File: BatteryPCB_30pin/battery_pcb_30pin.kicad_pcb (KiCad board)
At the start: 2 copper layers, 145.3 x 142.5 mm, 53 parts, among them J1 ESP32 left, J2 ESP32 right, J3 RunCam Split 4, J5 to COTS altimeter, J6 to SRAD flight computer, Q1 AO3407A, SW1 CAM POWER, SW2 COTS ARM, SW3 SRAD ARM, U1 LMR51430XFDDCR

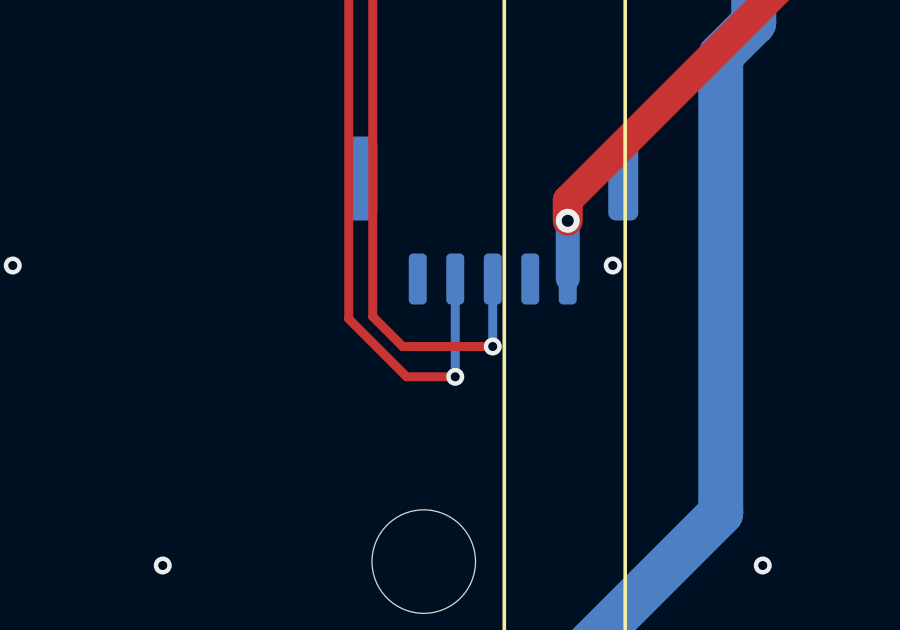
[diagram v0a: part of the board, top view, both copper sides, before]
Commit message: Battery PCB 30-pin: J3 pin order matches the RunCam Split 4 pads
J3 pins 3 and 5 swapped (3 = CAM_VIDEO, 5 = CAM_RX), so J3 pin 1..5 =
VCC, GND, Video, TX, RX, the camera's own pad order: the camera harness
is now a straight cable with no crossed wires.

- Schematic sheet 3 and the board pad nets updated; CAM_RX now drops to
  the back right beside pin 5 (route 2.5 mm shorter, old via removed).
- Back-silk legend reads 3 VID / 4 TX / 5 RX; README harness table, BOM
  camera note and hand-fit list updated; Gerbers, order-package zip,
  schematic PDF, project zip and STEP regenerated.
- ERC 0 errors, DRC 0 (schematic parity, zones refilled, same 3
  exclusions), verify_A unchanged, all 27 CPL placements re-checked.

BatteryPCB (the 38-pin board) keeps its old J3 order.

Co-Authored-By: Claude Opus 5.5 <noreply@anthropic.com>
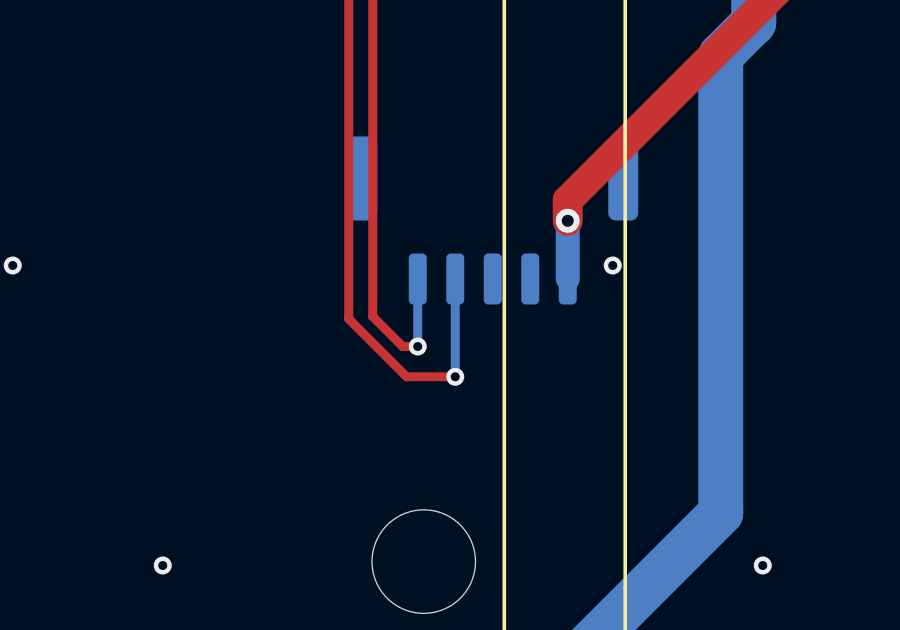
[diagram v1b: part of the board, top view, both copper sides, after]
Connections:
- J3 pad 3: /3. ESP32 + camera/CAM_RX -> /3. ESP32 + camera/CAM_VIDEO
- J3 pad 5: /3. ESP32 + camera/CAM_VIDEO -> /3. ESP32 + camera/CAM_RX
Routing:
- net /3. ESP32 + camera/CAM_RX: track 43.8 -> 41.3 mm
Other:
- board text added: "1 +5V 2 GND 3 VID 4 TX 5 RX"
- board text removed: "1 +5V 2 GND 3 RX 4 TX 5 VID"
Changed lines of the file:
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@@
 			(layers "B.Cu" "B.Mask" "B.Paste")
 			(roundrect_rratio 0.25)
-			(net "/3. ESP32 + camera/CAM_RX")
+			(net "/3. ESP32 + camera/CAM_VIDEO")
 			(pinfunction "Pin_3_3")
 			(pintype "passive")
@@
 			(layers "B.Cu" "B.Mask" "B.Paste")
 			(roundrect_rratio 0.25)
-			(net "/3. ESP32 + camera/CAM_VIDEO")
+			(net "/3. ESP32 + camera/CAM_RX")
 			(pinfunction "Pin_5_5")
 			(pintype "passive")
@@
 		)
 	)
-	(gr_text "1 +5V  2 GND\n3 RX  4 TX  5 VID"
+	(gr_text "1 +5V  2 GND\n3 VID  4 TX  5 RX"
 		(at 151.5 177.7 0)
 		(layer "B.SilkS")
@@
 	)
 	(segment
-		(start 142 135.845)
-		(end 142 171.7)
+		(start 141.2 138.395)
+		(end 141.2 171.78)
 		(width 0.3)
 		(layer "F.Cu")
-		(net "/3. ESP32 + camera/CAM_RX")
+		(net "/3. ESP32 + camera/CAM_TX")
 	)
 	(segment
-		(start 142 171.7)
-		(end 143 172.7)
+		(start 141.2 171.78)
+		(end 143.13 173.71)
 		(width 0.3)
 		(layer "F.Cu")
-		(net "/3. ESP32 + camera/CAM_RX")
+		(net "/3. ESP32 + camera/CAM_TX")
 	)
 	(segment
-		(start 143 172.7)
-		(end 146 172.7)
+		(start 143.13 173.71)
+		(end 144.75 173.71)
 		(width 0.3)
 		(layer "F.Cu")
-		(net "/3. ESP32 + camera/CAM_RX")
+		(net "/3. ESP32 + camera/CAM_TX")
 	)
 	(via
-		(at 142 135.845)
+		(at 144.75 173.71)
 		(size 0.6)
 		(drill 0.3)
 		(layers "F.Cu" "B.Cu")
-		(net "/3. ESP32 + camera/CAM_RX")
+		(net "/3. ESP32 + camera/CAM_TX")
 	)
 	(via
-		(at 146 172.7)
+		(at 141.2 138.395)
 		(size 0.6)
 		(drill 0.3)
 		(layers "F.Cu" "B.Cu")
-		(net "/3. ESP32 + camera/CAM_RX")
+		(net "/3. ESP32 + camera/CAM_TX")
 	)
 	(segment
-		(start 146 172.7)
-		(end 146 170.45)
+		(start 142.975 137.74)
+		(end 141.855 137.74)
 		(width 0.3)
 		(layer "B.Cu")
-		(net "/3. ESP32 + camera/CAM_RX")
+		(net "/3. ESP32 + camera/CAM_TX")
 	)
 	(segment
-		(start 142.975 135.2)
-		(end 142.645 135.2)
+		(start 141.855 137.74)
+		(end 141.2 138.395)
 		(width 0.3)
 		(layer "B.Cu")
-		(net "/3. ESP32 + camera/CAM_RX")
+		(net "/3. ESP32 + camera/CAM_TX")
 	)
 	(segment
-		(start 142.645 135.2)
-		(end 142 135.845)
+		(start 144.75 173.71)
+		(end 144.75 170.45)
 		(width 0.3)
 		(layer "B.Cu")
-		(net "/3. ESP32 + camera/CAM_RX")
+		(net "/3. ESP32 + camera/CAM_TX")
 	)
 	(segment
-		(start 141.2 138.395)
-		(end 141.2 171.78)
+		(start 142 135.845)
+		(end 142 171.7)
 		(width 0.3)
 		(layer "F.Cu")
-		(net "/3. ESP32 + camera/CAM_TX")
+		(net "/3. ESP32 + camera/CAM_RX")
 	)
 	(segment
-		(start 141.2 171.78)
-		(end 143.13 173.71)
+		(start 142 171.7)
+		(end 143 172.7)
 		(width 0.3)
 		(layer "F.Cu")
-		(net "/3. ESP32 + camera/CAM_TX")
+		(net "/3. ESP32 + camera/CAM_RX")
 	)
 	(segment
-		(start 143.13 173.71)
-		(end 144.75 173.71)
+		(start 143 172.7)
+		(end 143.5 172.7)
 		(width 0.3)
 		(layer "F.Cu")
-		(net "/3. ESP32 + camera/CAM_TX")
+		(net "/3. ESP32 + camera/CAM_RX")
 	)
 	(via
-		(at 144.75 173.71)
+		(at 142 135.845)
 		(size 0.6)
 		(drill 0.3)
 		(layers "F.Cu" "B.Cu")
-		(net "/3. ESP32 + camera/CAM_TX")
+		(net "/3. ESP32 + camera/CAM_RX")
 	)
 	(via
-		(at 141.2 138.395)
+		(at 143.5 172.7)
 		(size 0.6)
 		(drill 0.3)
 		(layers "F.Cu" "B.Cu")
-		(net "/3. ESP32 + camera/CAM_TX")
+		(net "/3. ESP32 + camera/CAM_RX")
 	)
 	(segment
-		(start 142.975 137.74)
-		(end 141.855 137.74)
+		(start 143.5 172.7)
+		(end 143.5 170.45)
 		(width 0.3)
 		(layer "B.Cu")
-		(net "/3. ESP32 + camera/CAM_TX")
+		(net "/3. ESP32 + camera/CAM_RX")
 	)
 	(segment
-		(start 141.855 137.74)
-		(end 141.2 138.395)
+		(start 142.975 135.2)
+		(end 142.645 135.2)
 		(width 0.3)
 		(layer "B.Cu")
-		(net "/3. ESP32 + camera/CAM_TX")
+		(net "/3. ESP32 + camera/CAM_RX")
 	)
 	(segment
-		(start 144.75 173.71)
-		(end 144.75 170.45)
+		(start 142.645 135.2)
+		(end 142 135.845)
 		(width 0.3)
 		(layer "B.Cu")
-		(net "/3. ESP32 + camera/CAM_TX")
+		(net "/3. ESP32 + camera/CAM_RX")
 	)
 	(segment

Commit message: Battery PCB 30-pin: test-point block on the right edge (5V, GND, COTS +/-, SRAD +/-)
Six through-hole test points together on the front right edge, between
the right rod's washer keep-out and the lower zip-tie cut-out, labelled
on the silk: top row TP1 +5V, TP5 COTS +, TP7 SRAD +; bottom row TP3 GND,
TP6 COTS -, TP8 SRAD -.

- TP1/TP3 moved out of the BT3/BT4 gap (hard to reach with cells in).
- TP5-TP8 are new (schematic sheet 4): the COTS and SRAD cells are
  isolated from GND, so each gets its own + / - pair, before the pin
  switch, so they read the cell whether armed or not.
- Routing: +5V from J1-15 (front, via at (44, 2), back); COTS/SRAD +
  from the top tabs down a channel beside BT4; COTS - (front) and
  SRAD - (back) from the bottom tabs under the zip-tie cut-out. Battery
  traces 1.0 mm (Pyro rules), +5V 0.8 mm.
- GND stitching: 3 vias removed where the block sits, 4 nudged <= 0.7 mm
  for clearance. Old TP1 feed removed; 'for zipties' label moved.
- verify_A checks all eight test points; README, layout notes and the
  order package's assembly scope updated; Gerbers, PDF, project zip and
  STEP regenerated. BOM and JLC files unchanged (test points are pads).

ERC 0 errors, DRC 0 (schematic parity, zones refilled, same 3
documented exclusions). No other part, trace or dimension changed.

Co-Authored-By: Claude Opus 5.5 <noreply@anthropic.com>
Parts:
- added TP5: TP_COTS+, TestPoint:TestPoint_THTPad_D2.0mm_Drill1.0mm, F.Cu at (206.5, 165.5)
- added TP6: TP_COTS-, TestPoint:TestPoint_THTPad_D2.0mm_Drill1.0mm, F.Cu at (206.5, 170.5)
- added TP7: TP_SRAD+, TestPoint:TestPoint_THTPad_D2.0mm_Drill1.0mm, F.Cu at (211.5, 165.5)
- added TP8: TP_SRAD-, TestPoint:TestPoint_THTPad_D2.0mm_Drill1.0mm, F.Cu at (211.5, 170.5)
- moved TP1 29.3 mm to (201.5, 165.5)
- moved TP3 27.7 mm to (201.5, 170.5)
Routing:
- net /4. COTS / SRAD supplies/COTS_BAT+: track 25.3 -> 118.7 mm
- net /4. COTS / SRAD supplies/SRAD_BAT+: track 14.3 -> 87.2 mm
- net /4. COTS / SRAD supplies/COTS_BAT-: track 17.7 -> 73.7 mm
- net /4. COTS / SRAD supplies/SRAD_BAT-: track 9.97 -> 45.9 mm, vias 0 -> 1
- net /2. Buck to 5 V/+5V: track 70.5 -> 102.5 mm, vias 3 -> 4
- net GND: vias 108 -> 105
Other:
- board text added: "COTS+"
- board text added: "COTS-"
- board text added: "SRAD+"
- board text added: "SRAD-"

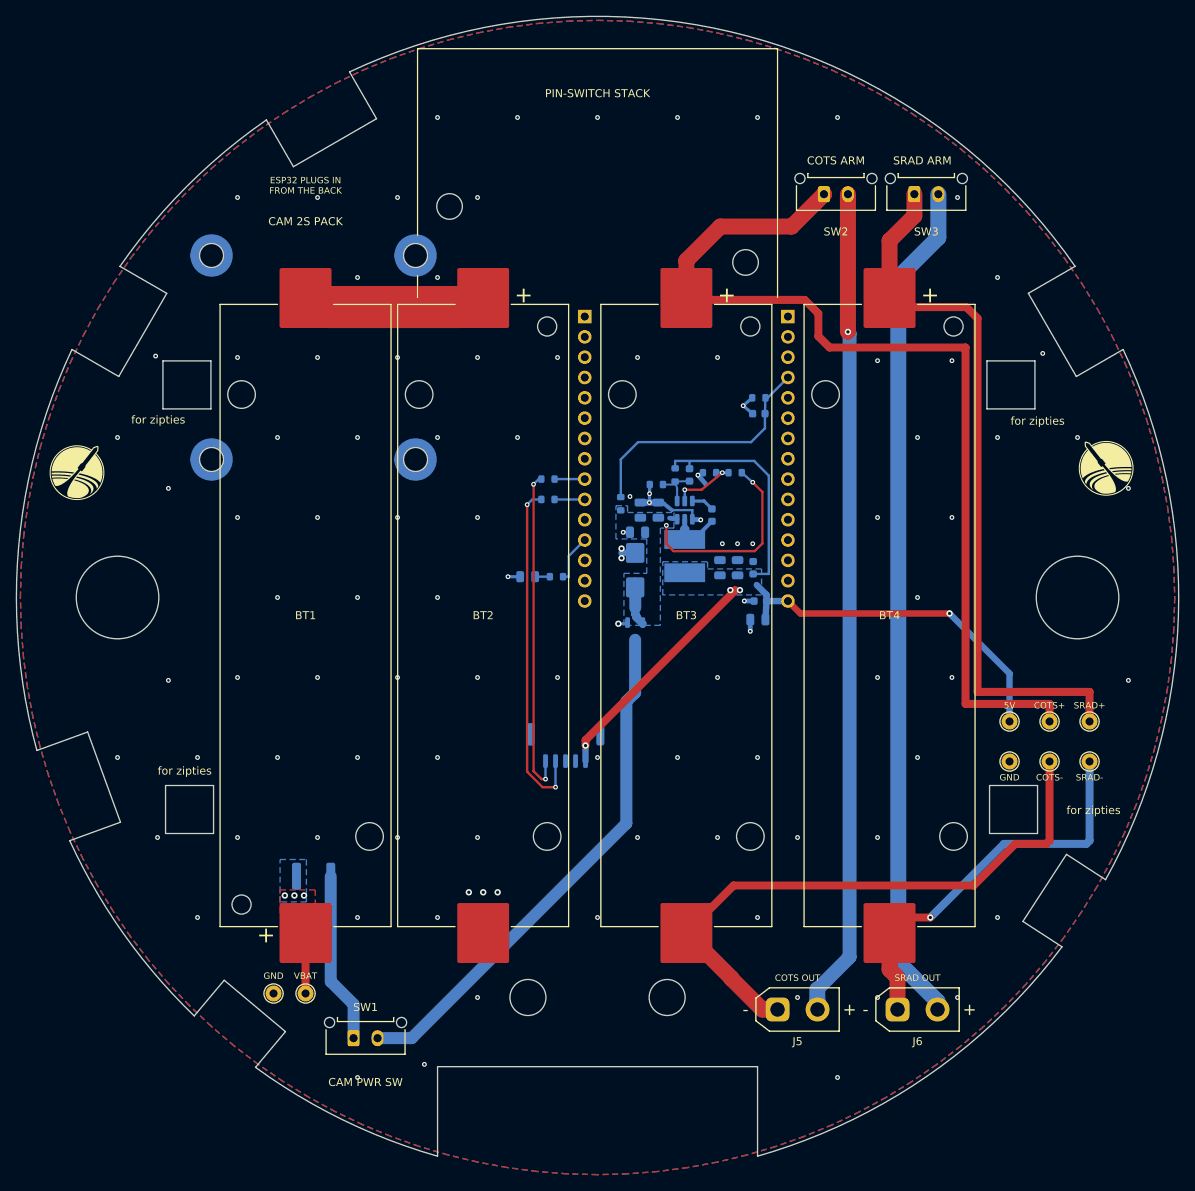
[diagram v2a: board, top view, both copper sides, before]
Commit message: Battery PCB 30-pin: XT30 and battery-holder holes to the datasheets; notes, check script
- XT30 J5/J6 pin holes 1.8 -> 1.9 mm (Amass drawing: 1.9 mm for the
  1.6 mm pins); 0.55 mm copper ring left on the 3.0 mm pads.
- Keystone 1042 holder peg holes 3.45 -> 3.5 mm and locator hole
  2.39 -> 2.4 mm on BT1-BT4 (Keystone M65p27; positions unchanged).
  Footprints updated in battery_pcb.pretty and on the board.
- Only those 16 hole sizes changed on the board: no part, trace, via,
  outline or silk moved. Tightest new gap: COTS_SW to a BT4 peg hole
  0.375 mm (rule 0.3).
- Schematic notes brought up to date: Q1 drop ~0.05 V (was 0.35 V from
  the old diode), J5/J6 are XT30 not Micro-Fit, C9/C10 sit at the
  ESP32's VIN (J1-15).
- verify_A: the old "seven edge cut-outs" count is replaced by a real
  check (7 rim notches + 4 square zip-tie cut-outs); ALL PASS, 36 checks.
- Gerbers, order-package zip, schematic PDF, project zip and STEP
  regenerated; BOM and CPL unchanged.

ERC 0 errors, DRC 0 (schematic parity, zones refilled, same 3
documented exclusions).

Co-Authored-By: Claude Opus 5.5 <noreply@anthropic.com>
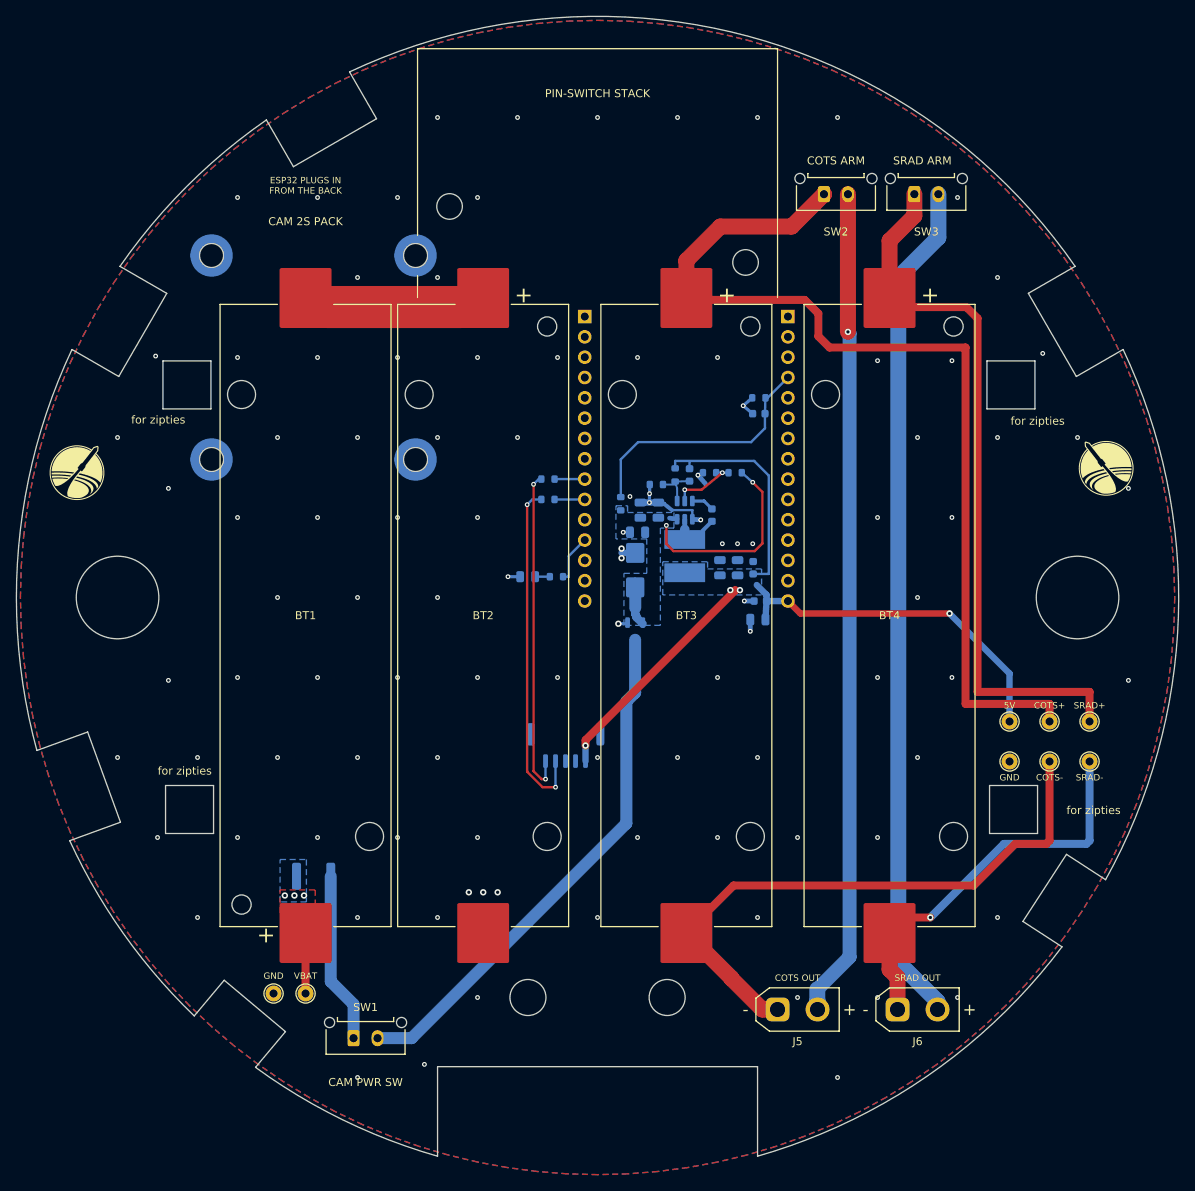
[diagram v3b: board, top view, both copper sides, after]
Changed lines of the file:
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@@
 		(pad "" np_thru_hole circle
 			(at -36.13 -8 90)
-			(size 2.39 2.39)
-			(drill 2.39)
+			(size 2.4 2.4)
+			(drill 2.4)
 			(layers "*.Cu" "*.Mask")
 		)
 		(pad "" np_thru_hole circle
 			(at -27.62 8 90)
-			(size 3.45 3.45)
-			(drill 3.45)
+			(size 3.5 3.5)
+			(drill 3.5)
 			(layers "*.Cu" "*.Mask")
 		)
 		(pad "" np_thru_hole circle
 			(at 27.62 -8 90)
-			(size 3.45 3.45)
-			(drill 3.45)
+			(size 3.5 3.5)
+			(drill 3.5)
 			(layers "*.Cu" "*.Mask")
 		)
@@
 		(pad "" np_thru_hole circle
 			(at -36.13 -8 270)
-			(size 2.39 2.39)
-			(drill 2.39)
+			(size 2.4 2.4)
+			(drill 2.4)
 			(layers "*.Cu" "*.Mask")
 		)
 		(pad "" np_thru_hole circle
 			(at -27.62 8 270)
-			(size 3.45 3.45)
-			(drill 3.45)
+			(size 3.5 3.5)
+			(drill 3.5)
 			(layers "*.Cu" "*.Mask")
 		)
 		(pad "" np_thru_hole circle
 			(at 27.62 -8 270)
-			(size 3.45 3.45)
-			(drill 3.45)
+			(size 3.5 3.5)
+			(drill 3.5)
 			(layers "*.Cu" "*.Mask")
 		)
@@
 			(at 0 0)
 			(size 3 3)
-			(drill 1.8)
+			(drill 1.9)
 			(layers "*.Cu" "*.Mask")
 			(remove_unused_layers no)
@@
 			(at 5 0)
 			(size 3 3)
-			(drill 1.8)
+			(drill 1.9)
 			(layers "*.Cu" "*.Mask")
 			(remove_unused_layers no)
@@
 		(pad "" np_thru_hole circle
 			(at -36.13 -8 270)
-			(size 2.39 2.39)
-			(drill 2.39)
+			(size 2.4 2.4)
+			(drill 2.4)
 			(layers "*.Cu" "*.Mask")
 		)
 		(pad "" np_thru_hole circle
 			(at -27.62 8 270)
-			(size 3.45 3.45)
-			(drill 3.45)
+			(size 3.5 3.5)
+			(drill 3.5)
 			(layers "*.Cu" "*.Mask")
 		)
 		(pad "" np_thru_hole circle
 			(at 27.62 -8 270)
-			(size 3.45 3.45)
-			(drill 3.45)
+			(size 3.5 3.5)
+			(drill 3.5)
 			(layers "*.Cu" "*.Mask")
 		)
@@
 			(at 0 0)
 			(size 3 3)
-			(drill 1.8)
+			(drill 1.9)
 			(layers "*.Cu" "*.Mask")
 			(remove_unused_layers no)
@@
 			(at 5 0)
 			(size 3 3)
-			(drill 1.8)
+			(drill 1.9)
 			(layers "*.Cu" "*.Mask")
 			(remove_unused_layers no)
@@
 		(pad "" np_thru_hole circle
 			(at -36.13 -8 270)
-			(size 2.39 2.39)
-			(drill 2.39)
+			(size 2.4 2.4)
+			(drill 2.4)
 			(layers "*.Cu" "*.Mask")
 		)
 		(pad "" np_thru_hole circle
 			(at -27.62 8 270)
-			(size 3.45 3.45)
-			(drill 3.45)
+			(size 3.5 3.5)
+			(drill 3.5)
 			(layers "*.Cu" "*.Mask")
 		)
 		(pad "" np_thru_hole circle
 			(at 27.62 -8 270)
-			(size 3.45 3.45)
-			(drill 3.45)
+			(size 3.5 3.5)
+			(drill 3.5)
 			(layers "*.Cu" "*.Mask")
 		)
